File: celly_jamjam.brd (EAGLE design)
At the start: 100 x 80 mm, 58 parts, among them T1 2N3904, U1 OSCILLATOR5X3

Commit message: finished schematic, now onto board. jeeez
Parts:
- removed ICL7660: (no value), ic-package:DIL08
- added FERRITEBEADLEAD: type43, inductors:0402
- added IC1: M3500-1324S/T, burr-brown:SOT23-5
- added MICROSTRIPLINE, MICROSTRIPLN2: 50 Ohm, inductors:0402
- added RFOUTPUTANTENNA: 80mW, SparkFun-RF:ANTENNA-CHIP
- moved 1MEG 285.1 mm to (96.5, 58.4)
- moved C22 275.8 mm to (88.9, 71.1)
- moved C23 275.8 mm to (88.9, 40.6)
- moved NOISEAMP 275.8 mm to (88.9, 30.5)
- moved R23 275.8 mm to (87.6, 74.9)
- moved R24 275.8 mm to (87.6, 67.3)
- moved R25 275.8 mm to (87.6, 63.5)
- moved R28 275.8 mm to (88.9, 45.7)
- moved L2 255.5 mm to (52.1, 6.35)
- moved U1 247.7 mm to (67.3, 3.81), turned to 180 degrees
- moved TRANSISTOR 243.0 mm to (31.8, 6.35)
- moved SWEEPAMP 239.0 mm to (94.0, 11.4), turned to 180 degrees
- moved LM1458 237.0 mm to (55.9, 71.1)
- moved TRIWAVGEN 196.7 mm to (95.2, 3.81), turned to 90 degrees
- moved C1 186.5 mm to (69.8, 80.0)
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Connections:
- new net N$33: C9.1, IC1.3
- new net N$34: MICROSTRIPLN2.2, RFOUTPUTANTENNA.FEED
- new net N$35: C9.2, MICROSTRIPLINE.2
- new net N$36: FERRITEBEADLEAD.2, R16.1
- new net N$37: MICROSTRIPLN2.1
- net GND: now also IC1.2, IC1.5, RFOUTPUTANTENNA.GND; no longer ICL7660.3
- net N$17: now also IC1.1
- net N$2: now also FERRITEBEADLEAD.1; no longer R16.1
- net N$28: now also MICROSTRIPLINE.1
- net N$4: now also C17.A, VOLTAGEINVERT.2; no longer C17.C, ICL7660.4
- net N$5: now also C17.C, VOLTAGEINVERT.4; no longer C17.A, ICL7660.2
- net N$7: now also VOLTAGEINVERT.5; no longer ICL7660.5
- net V+: no longer VOLTAGEINVERT.8
- net VCC: now also VOLTAGEINVERT.1, VOLTAGEINVERT.8; no longer ICL7660.1, ICL7660.8
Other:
- board size 100 x 80 mm -> 100 x 82.5 mm

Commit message: design is better
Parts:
- removed MICROSTRIPLN2: 50 Ohm, inductors:0402
- removed TRANSISTOR: MPF102, transistor-small-signal:SOT23
- added MICROSTRIPLINE1: 50 Ohm, inductors:0402
- added Q1: mpf102, transistor-fet:TO92
- C10, C9: value (none) -> 68pF
- C12: value (none) -> 0.1uF
- IC1: value M3500-1324S/T -> AG603-86
- U1: value OSCILLATOR5X3 -> M3500
- moved TRIWAVGEN 84.6 mm to (39.5, 67.5)
- moved 1MEG 82.2 mm to (14.8, 68.1), turned to 90 degrees
- moved RFOUTPUTANTENNA 74.1 mm to (78.6, 38.5), turned to 180 degrees
- moved R25 68.4 mm to (19.4, 68.2), turned to 90 degrees
- moved SWEEPAMP 68.1 mm to (45.9, 59.7)
- moved C19 66.5 mm to (20.6, 72.5), turned to 270 degrees
- moved R3 61.3 mm to (28.3, 69.1), turned to 180 degrees
- moved C18 60.3 mm to (25.5, 72.5), turned to 270 degrees
- moved C2 59.4 mm to (17.1, 50.2), turned to 180 degrees
- moved L1 58.9 mm to (71.3, 42.4), turned to 90 degrees
- moved C1 58.0 mm to (14.8, 61.5), turned to 270 degrees
- moved NOISEAMP 57.7 mm to (35.0, 51.1), turned to 90 degrees
- moved C16 56.7 mm to (16.0, 53.9), turned to 180 degrees
- moved IC1 56.6 mm to (66.1, 55.1), turned to 270 degrees
- moved L2 56.3 mm to (61.2, 61.9), turned to 90 degrees
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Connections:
- removed net N$34 (its old number): MICROSTRIPLN2.2, RFOUTPUTANTENNA.FEED
- removed net N$37: MICROSTRIPLN2.1
- new net N$17: C10.1, MICROSTRIPLINE1.1
- new net N$40: MICROSTRIPLINE1.2, RFOUTPUTANTENNA.FEED
- net N$24: now also Q1.3; no longer TRANSISTOR.3
- net N$27: now also Q1.1; no longer TRANSISTOR.1
- net N$30: now also Q1.2; no longer TRANSISTOR.2
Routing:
- net GND: track 0.00 -> 44.6 mm
- net VCC: track 0.00 -> 26.6 mm
- net N$3: track 0.00 -> 21.0 mm
- net N$13: track 0.00 -> 20.5 mm
- net N$32: track 0.00 -> 15.6 mm
- net N$36: track 0.00 -> 12.8 mm
- net N$24: track 0.00 -> 11.4 mm
- net N$19: track 0.00 -> 11.3 mm
- net N$26: track 0.00 -> 9.98 mm
- net N$14: track 0.00 -> 9.51 mm
- net N$34: track 0.00 -> 9.41 mm
- net N$2: track 0.00 -> 9.09 mm
- net N$20: track 0.00 -> 8.79 mm
- net N$8: track 0.00 -> 8.28 mm
- net N$27: track 0.00 -> 8.14 mm
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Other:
- board size 100 x 82.5 mm -> 117.8 x 83.8 mm

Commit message: added correct VCO
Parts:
- removed C5: 0.1uF, SparkFun-Passives:0603-CAP
- removed U1: M3500, SparkFun-FreqCtrl:CRYSTAL-SMD-5X3
- added C24: 0.1uF, SparkFun-Passives:0603-CAP
- added U$1: CVCO55CL, crystec_vco:CVCO55CL
- L1: value 10uH -> 10nh
- moved L1 62.0 mm to (15.5, 15.5), turned to 0 degrees
- moved C6 55.8 mm to (21.5, 15.5), turned to 0 degrees
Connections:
- new net N$37: C24.2, L1.2, U$1.P$14
- net GND: now also C24.1, C6.1, U$1.P$7; no longer C5.1, C6.2, U1.2
- net N$29: no longer U1.3
- net N$3: now also U$1.P$10; no longer C20.A, C6.1, L1.2, U1.4
- net N$32: now also U$1.P$2; no longer U1.1
- net VCC: now also C20.A, C6.2; no longer C5.2
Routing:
- net N$3: track 21.0 -> 0.00 mm
- net VCC: track 26.6 -> 19.3 mm
- net N$16: track 0.00 -> 5.30 mm
- net GND: track 44.6 -> 40.6 mm

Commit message: added VCO, changed design. still needs a lot of work
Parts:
- moved C6 31.3 mm to (14.5, 46.0), turned to 180 degrees
- moved L1 22.1 mm to (14.0, 37.5), turned to 90 degrees
- moved C24 20.6 mm to (20.5, 41.0), turned to 180 degrees
- moved U$1 7.00 mm to (18.5, 21.5)
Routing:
- net N$32: track 15.5 -> 55.2 mm
- net VCC: track 19.3 -> 39.5 mm
- net N$37: track 0.00 -> 18.7 mm
- net GND: track 40.6 -> 41.4 mm
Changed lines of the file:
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@@
 <element name="C10" library="SparkFun-Passives" package="0603-CAP" value="68pF" x="64.5" y="59" rot="R180"/>
 <element name="Q1" library="transistor-fet" package="TO92" value="mpf102" x="51" y="47"/>
-<element name="U$1" library="crystec_vco" package="CVCO55CL" value="CVCO55CL" x="18.5" y="28.5"/>
-<element name="C24" library="SparkFun-Passives" package="0603-CAP" value="0.1uF" x="10.5" y="23"/>
-<element name="C6" library="SparkFun-Passives" package="0603-CAP" value="0.1uF" x="21.5" y="15.5"/>
-<element name="L1" library="SparkFun-Passives" package="0603" value="10nh" x="15.5" y="15.5"/>
+<element name="U$1" library="crystec_vco" package="CVCO55CL" value="CVCO55CL" x="18.5" y="21.5"/>
+<element name="C24" library="SparkFun-Passives" package="0603-CAP" value="0.1uF" x="20.5" y="41" rot="R180"/>
+<element name="C6" library="SparkFun-Passives" package="0603-CAP" value="0.1uF" x="14.5" y="46" rot="R180"/>
+<element name="L1" library="SparkFun-Passives" package="0603" value="10nh" x="14" y="37.5" rot="R90"/>
 </elements>
 <signals>
@@
 <wire x1="26.8534" y1="52.575" x2="34.21" y2="55.21" width="0" layer="19" extent="1-1"/>
 <wire x1="19.41" y1="58.82" x2="26.8534" y2="52.575" width="0" layer="19" extent="1-1"/>
+<wire x1="15.35" y1="46" x2="15.28" y2="50.22" width="0" layer="19" extent="1-1"/>
 <wire x1="44.345" y1="35.09" x2="40.52" y2="46.45" width="0" layer="19" extent="1-1"/>
 <wire x1="45.615" y1="35.09" x2="44.345" y2="35.09" width="0" layer="19" extent="1-1"/>
+<wire x1="31.2" y1="29.247" x2="44.345" y2="35.09" width="0" layer="19" extent="1-1"/>
 <wire x1="20.62" y1="73.88" x2="14.85" y2="60.64" width="0" layer="19" extent="1-1"/>
-<wire x1="31.2" y1="36.247" x2="44.345" y2="35.09" width="0" layer="19" extent="1-1"/>
-<wire x1="9.65" y1="23" x2="31.2" y2="36.247" width="0" layer="19" extent="1-1"/>
-<wire x1="20.65" y1="15.5" x2="9.65" y2="23" width="0" layer="19" extent="1-1"/>
+<wire x1="21.35" y1="41" x2="21.5" y2="41" width="0.4064" layer="1"/>
+<wire x1="21.5" y1="41" x2="22" y2="41.5" width="0.4064" layer="1"/>
+<wire x1="22" y1="41.5" x2="15.35" y2="46" width="0" layer="19" extent="1-16"/>
 </signal>
 <signal name="VCC">
@@
 <contactref element="C6" pad="2"/>
 <contactref element="C20" pad="A"/>
+<wire x1="18.135" y1="50.035" x2="18.135" y2="48.135" width="0.4064" layer="1"/>
+<wire x1="18.135" y1="48.135" x2="18" y2="48" width="0.4064" layer="1"/>
+<wire x1="18" y1="48" x2="13.5" y2="48" width="0.4064" layer="1"/>
+<wire x1="13.5" y1="48" x2="13.5" y2="46.15" width="0.4064" layer="1"/>
+<wire x1="13.5" y1="46.15" x2="13.65" y2="46" width="0.4064" layer="1"/>
+<wire x1="13.65" y1="46" x2="13.65" y2="41.15" width="0.4064" layer="1"/>
+<wire x1="13.65" y1="41.15" x2="12.5" y2="40" width="0.4064" layer="1"/>
+<wire x1="12.5" y1="40" x2="12.5" y2="36.5" width="0.4064" layer="1"/>
+<wire x1="12.5" y1="36.5" x2="13.85" y2="36.5" width="0.4064" layer="1"/>
+<wire x1="13.85" y1="36.5" x2="14" y2="36.65" width="0.4064" layer="1"/>
 <wire x1="71.17" y1="49.015" x2="67.52" y2="60.76" width="0" layer="19" extent="1-1"/>
 <wire x1="72.78" y1="46.89" x2="71.17" y2="49.015" width="0" layer="19" extent="1-1"/>
@@
 <wire x1="30.82" y1="64.84" x2="26.8534" y2="50.035" width="0" layer="19" extent="1-1"/>
 <wire x1="30.94" y1="71.06" x2="30.94" y2="64.96" width="0" layer="19" extent="1-1"/>
-<wire x1="22.35" y1="15.5" x2="47.99" y2="30.2" width="0" layer="19" extent="1-1"/>
-<wire x1="14.65" y1="15.5" x2="22.35" y2="15.5" width="0" layer="19" extent="1-1"/>
 </signal>
 <signal name="V+">
@@
 <contactref element="C3" pad="2"/>
 <contactref element="R3" pad="1"/>
-<wire x1="29.16" y1="69.09" x2="30.82" y2="59.76" width="0" layer="19" extent="1-1"/>
 <wire x1="36.1" y1="60.14" x2="31.2" y2="60.14" width="0.4064" layer="1"/>
 <wire x1="31.2" y1="60.14" x2="30.82" y2="59.76" width="0.4064" layer="1"/>
 <wire x1="40.17" y1="60.14" x2="36.1" y2="60.14" width="0.4064" layer="1"/>
+<wire x1="31.2" y1="60.14" x2="29.16" y2="69.09" width="0" layer="19" extent="1-1"/>
 </signal>
 <signal name="N$8">
@@
 <contactref element="1MEG" pad="8"/>
 <contactref element="1MEG" pad="6"/>
-<wire x1="19.39" y1="69.04" x2="23.2" y2="64.84" width="0" layer="19" extent="1-1"/>
+<wire x1="27.46" y1="69.09" x2="23.59" y2="69.09" width="0.4064" layer="1"/>
+<wire x1="23.59" y1="69.09" x2="23.5" y2="69" width="0.4064" layer="1"/>
+<wire x1="23.5" y1="69" x2="23.5" y2="65.14" width="0.4064" layer="1"/>
+<wire x1="23.5" y1="65.14" x2="23.2" y2="64.84" width="0.4064" layer="1"/>
 <wire x1="15.475" y1="69.27" x2="19.39" y2="69.04" width="0" layer="19" extent="1-1"/>
 <wire x1="15.475" y1="68.47" x2="15.475" y2="69.27" width="0" layer="19" extent="1-1"/>
@@
 <wire x1="14.225" y1="67.67" x2="14.225" y2="68.47" width="0" layer="19" extent="1-1"/>
 <wire x1="14.225" y1="66.87" x2="14.225" y2="67.67" width="0" layer="19" extent="1-1"/>
-<wire x1="27.46" y1="69.09" x2="23.59" y2="69.09" width="0.4064" layer="1"/>
-<wire x1="23.59" y1="69.09" x2="23.5" y2="69" width="0.4064" layer="1"/>
-<wire x1="23.5" y1="69" x2="23.5" y2="65.14" width="0.4064" layer="1"/>
-<wire x1="23.5" y1="65.14" x2="23.2" y2="64.84" width="0.4064" layer="1"/>
+<wire x1="23.5" y1="69" x2="19.39" y2="69.04" width="0" layer="19" extent="1-1"/>
 </signal>
 <signal name="N$10">
@@
 <contactref element="R18" pad="1"/>
 <contactref element="T1" pad="2"/>
-<wire x1="56.93" y1="29.23" x2="58.05" y2="33.595" width="0" layer="19" extent="1-1"/>
 <wire x1="53.82" y1="32.27" x2="53.82" y2="30.68" width="0.4064" layer="1"/>
 <wire x1="53.82" y1="30.68" x2="54" y2="30.5" width="0.4064" layer="1"/>
 <wire x1="54" y1="30.5" x2="55.66" y2="30.5" width="0.4064" layer="1"/>
 <wire x1="55.66" y1="30.5" x2="56.93" y2="29.23" width="0.4064" layer="1"/>
+<wire x1="55.66" y1="30.5" x2="58.05" y2="33.595" width="0" layer="19" extent="1-1"/>
 </signal>
 <signal name="N$21">
@@
 <contactref element="C15" pad="1"/>
 <contactref element="NOISEAMP" pad="2"/>
-<wire x1="35.605" y1="50.73" x2="38.13" y2="50.71" width="0" layer="19" extent="1-1"/>
 <wire x1="40.89" y1="49.79" x2="40.89" y2="50.11" width="0.4064" layer="1"/>
 <wire x1="40.89" y1="50.11" x2="40" y2="51" width="0.4064" layer="1"/>
 <wire x1="40" y1="51" x2="38.42" y2="51" width="0.4064" layer="1"/>
 <wire x1="38.42" y1="51" x2="38.13" y2="50.71" width="0.4064" layer="1"/>
+<wire x1="35.605" y1="50.73" x2="38.13" y2="50.71" width="0" layer="19" extent="1-1"/>
 </signal>
 <signal name="N$24">
@@
 <wire x1="56.96" y1="46.5" x2="56.92" y2="46.54" width="0.4064" layer="1"/>
 <contactref element="U$1" pad="P$2"/>
-<wire x1="23.961" y1="28.5" x2="52" y2="43.04" width="0" layer="19" extent="1-1"/>
+<wire x1="23.961" y1="21.5" x2="35" y2="21.5" width="0.4064" layer="1"/>
+<wire x1="35" y1="21.5" x2="51.5" y2="38" width="0.4064" layer="1"/>
+<wire x1="51.5" y1="38" x2="51.5" y2="42.54" width="0.4064" layer="1"/>
+<wire x1="51.5" y1="42.54" x2="52" y2="43.04" width="0.4064" layer="1"/>
 </signal>
 <signal name="N$31">
@@
 <contactref element="VOLTAGEINVERT" pad="5"/>
 <contactref element="LM1458" pad="4"/>
-<wire x1="20.7066" y1="53.845" x2="23.2" y2="57.22" width="0" layer="19" extent="1-1"/>
 <wire x1="20.7066" y1="53.845" x2="17.445" y2="53.845" width="0.4064" layer="1"/>
 <wire x1="17.445" y1="53.845" x2="17.39" y2="53.9" width="0.4064" layer="1"/>
+<wire x1="20.7066" y1="53.845" x2="23.2" y2="57.22" width="0" layer="19" extent="1-1"/>
 </signal>
 <signal name="N$17">
@@
 <contactref element="C4" pad="1"/>
 <contactref element="Q1" pad="2"/>
-<wire x1="51" y1="48.905" x2="56.92" y2="48.24" width="0" layer="19" extent="1-1"/>
 <wire x1="46.83" y1="53.13" x2="48.37" y2="53.13" width="0.4064" layer="1"/>
 <wire x1="48.37" y1="53.13" x2="51" y2="50.5" width="0.4064" layer="1"/>
 <wire x1="51" y1="50.5" x2="51" y2="48.905" width="0.4064" layer="1"/>
+<wire x1="51" y1="48.905" x2="56.92" y2="48.24" width="0" layer="19" extent="1-1"/>
 </signal>
 <signal name="N$27">
@@
 <contactref element="L1" pad="2"/>
 <contactref element="U$1" pad="P$14"/>
-<wire x1="11.35" y1="23" x2="16.35" y2="15.5" width="0" layer="19" extent="1-1"/>
-<wire x1="18.5" y1="36.501" x2="11.35" y2="23" width="0" layer="19" extent="1-1"/>
+<wire x1="19.65" y1="41" x2="16.65" y2="41" width="0.4064" layer="1"/>
+<wire x1="16.65" y1="41" x2="14" y2="38.35" width="0.4064" layer="1"/>
+<wire x1="14" y1="38.35" x2="14.65" y2="38.35" width="0.4064" layer="1"/>
+<wire x1="14.65" y1="38.35" x2="17" y2="36" width="0.4064" layer="1"/>
+<wire x1="17" y1="36" x2="17" y2="29.5" width="0.4064" layer="1"/>
+<wire x1="17" y1="29.5" x2="18.499" y2="29.5" width="0.4064" layer="1"/>
+<wire x1="18.499" y1="29.5" x2="18.5" y2="29.501" width="0.4064" layer="1"/>
 </signal>
 <signal name="N$3">

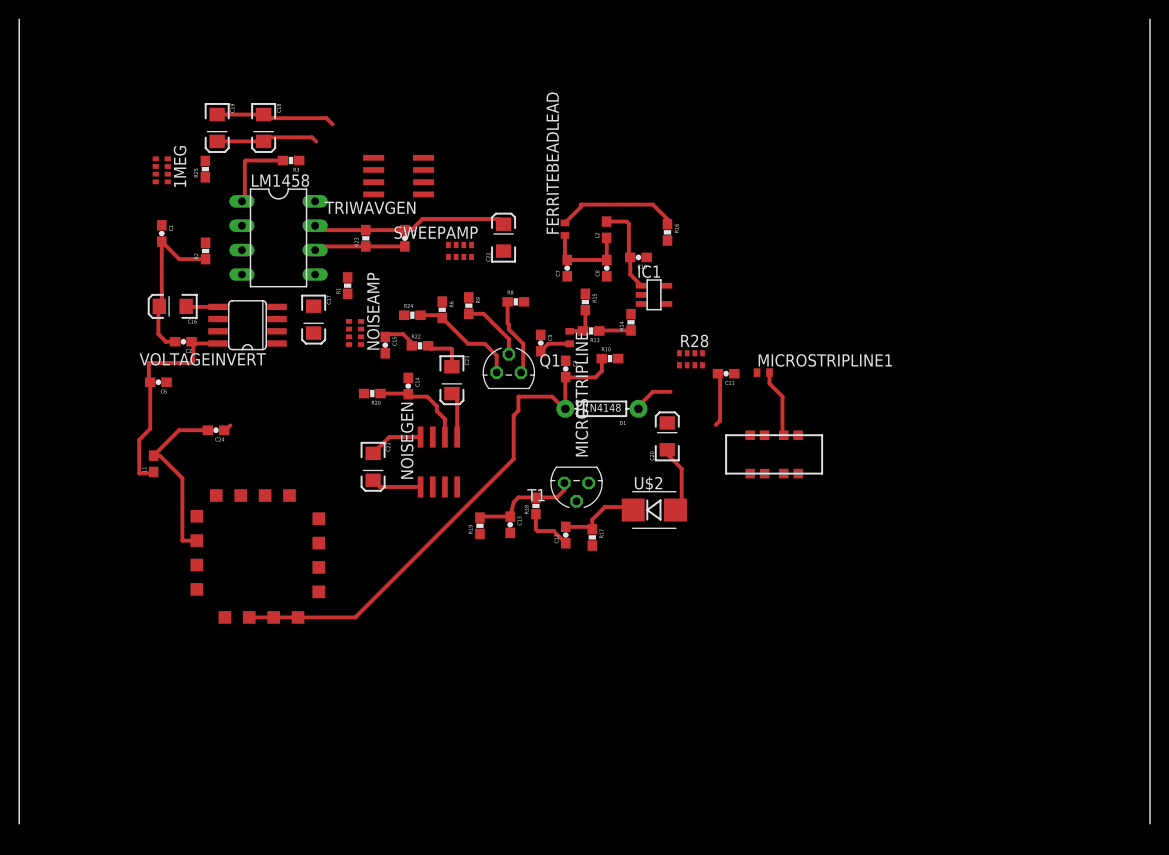
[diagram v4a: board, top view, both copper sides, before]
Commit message: changed everything to SMD. much work to be done
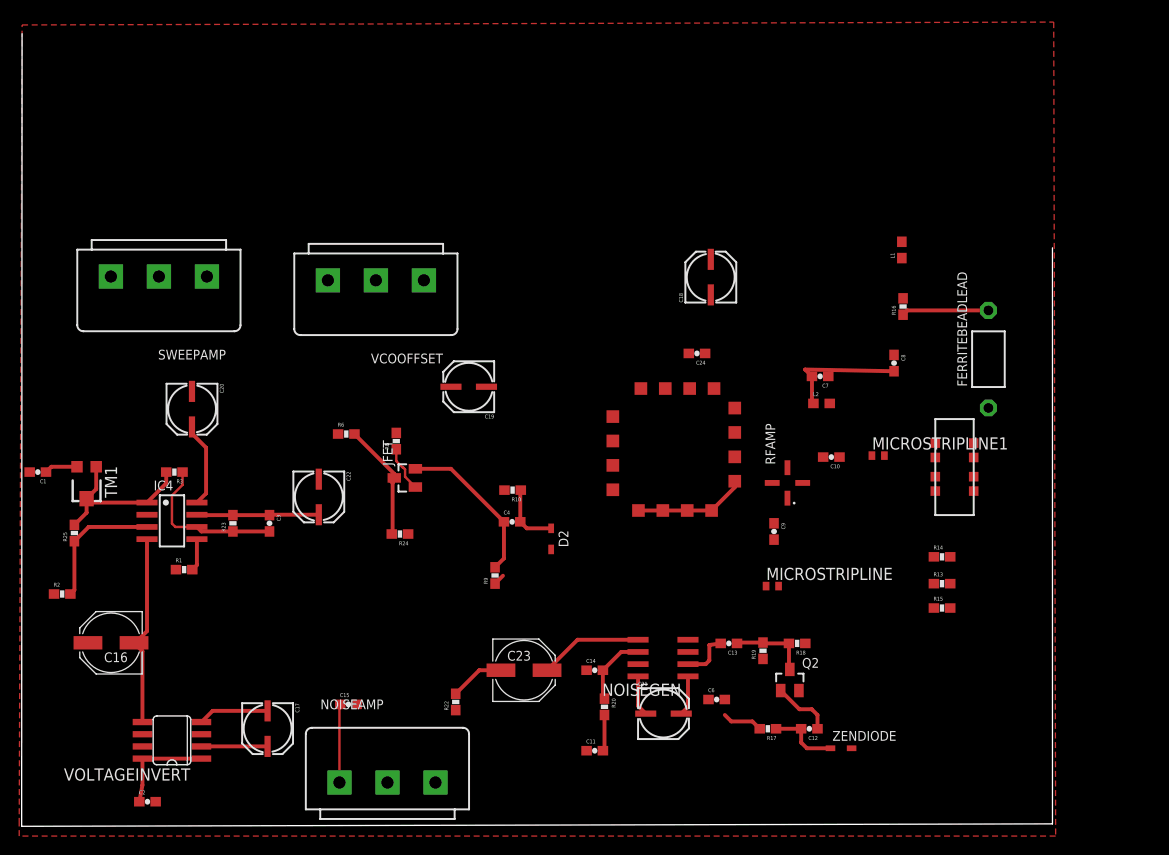
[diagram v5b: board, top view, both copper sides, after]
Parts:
- removed 1MEG, R28: POTENTIOMETER, SparkFun-Passives:0603-ARV
- removed D1: 1N4148, SparkFun-DiscreteSemi:DIODE-1N4148
- removed IC1: AG603-86, burr-brown:SOT23-5
- removed LM1458: (no value), ic-package:DIL08
- removed Q1: mpf102, transistor-fet:TO92
- removed T1: 2N3904, transistor:TO92
- removed TRIWAVGEN: LM1458D, linear:SO08
- removed U$2: DIODE-ZENERSMB, SparkFun-DiscreteSemi:SMB-DIODE
- added D2: 1N4148, zetex:SOD323
- added IC4: LM1458, linear:SO08
- added JFET: MMBF5484*, transistor-fet:SOT23
- added Q2: MMBT3904, transistor-npn:SOT23-BEC
- added RFAMP: ag603, mini-circuits:FG873
- added TM1: (no value), adafruit:TC33X
- added VCOOFFSET: 5K/10TURN, pot:P160KN
- added ZENDIODE: MMBZ5235BW, zetex:SOD323
- C16, C23: device SparkFun-Capacitors:EIA3216 -> SparkFun-Capacitors:PANASONIC_D
- C17, C18, C19, C20, C21, C22: device SparkFun-Capacitors:EIA3216 -> SparkFun-Capacitors:PANASONIC_C
- FERRITEBEADLEAD: device inductors:0402 -> inductor-jwmiller:FB-226
- NOISEAMP: value 5k/10turn -> 5K/10TURN; device SparkFun-Passives:0603-ARV -> pot:P160KN
- NOISEGEN: device linear:SO08 -> linear:SO08@1
- SWEEPAMP: device SparkFun-Passives:0603-ARV -> pot:P160KN
- moved L1 81.1 mm to (91.9, 59.8)
- moved C6 66.9 mm to (72.6, 13.0), turned to 0 degrees
- moved NOISEAMP 50.7 mm to (38.4, 0.51), turned to 270 degrees
- moved C24 50.7 mm to (70.6, 49.0)
- moved U$1 49.5 mm to (61.8, 45.3), turned to 270 degrees
- moved C20 49.4 mm to (18.2, 43.2), turned to 270 degrees
- moved R15 49.0 mm to (96.1, 22.5), turned to 0 degrees
- moved C18 48.9 mm to (71.8, 56.9), turned to 90 degrees
- moved C2 48.1 mm to (13.4, 2.31), turned to 0 degrees
- moved FERRITEBEADLEAD 46.1 mm to (100.9, 48.4)
- moved R13 45.0 mm to (96.1, 25.0), turned to 0 degrees
- moved VOLTAGEINVERT 44.0 mm to (15.9, 8.70)
- moved C17 42.8 mm to (26.1, 9.97)
- moved C11 41.6 mm to (59.9, 7.62), turned to 0 degrees
- moved R20 40.6 mm to (61.0, 12.2), turned to 270 degrees
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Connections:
- removed net N$1: LM1458.5, R1.2
- removed net N$13: C22.A, C3.1, LM1458.7, R23.2
- removed net N$9: LM1458.3, R2.2, R25.1
- removed net V+: TRIWAVGEN.8
- removed net V-: TRIWAVGEN.4
- new net N$47: JFET.3, R24.2, R6.2
- new net N$48: IC4.5, R1.2
- new net N$49: IC4.3, R2.2, R25.1
- new net VDD: C20.+, C6.2, L1.1
- net GND: now also C16.+, C18.-, C19.-, C20.-, D2.2, NOISEAMP.3, Q2.E, RFAMP.2, RFAMP.4, SWEEPAMP.1, U$1.P$1, U$1.P$11, U$1.P$12, U$1.P$13, U$1.P$15, U$1.P$16, U$1.P$3, U$1.P$4, U$1.P$5, U$1.P$6, U$1.P$8, U$1.P$9, VCOOFFSET.3, ZENDIODE.2; no longer C16.A, C18.C, C19.C, C20.C, D1.A, IC1.2, IC1.5, NOISEAMP.1, R28.2, SWEEPAMP.2, T1.3, U$2.A
- net N$10: now also IC4.2, TM1.3; no longer 1MEG.1, LM1458.2
- net N$11: now also SWEEPAMP.2; no longer SWEEPAMP.3, SWEEPAMP.4, SWEEPAMP.5, SWEEPAMP.6, SWEEPAMP.7, SWEEPAMP.8
- net N$12: now also C22.-, SWEEPAMP.3; no longer C22.C, SWEEPAMP.1
- net N$14: now also IC4.6; no longer LM1458.6
- net N$15: now also C21.-; no longer C21.C
- net N$16: now also Q2.B; no longer T1.2
- net N$19: now also Q2.C; no longer T1.1
- net N$20: now also ZENDIODE.1; no longer U$2.C
- net N$21: now also C23.-; no longer C23.C
- net N$22: now also C23.+; no longer C23.A
- net N$23: now also NOISEAMP.1; no longer NOISEAMP.2
- net N$24: now also C22.+, C3.1, IC4.7, R23.2; no longer Q1.3, R24.2, R6.2
- net N$25: now also NOISEAMP.2; no longer NOISEAMP.3, NOISEAMP.4, NOISEAMP.5, NOISEAMP.6, NOISEAMP.7, NOISEAMP.8
- net N$27: now also JFET.1; no longer Q1.1
- net N$30: now also JFET.2; no longer Q1.2
- net N$31: now also VCOOFFSET.2; no longer R28.3, R28.4, R28.5, R28.6, R28.7, R28.8
- net N$32: now also D2.1; no longer D1.C
- net N$33: now also RFAMP.1; no longer IC1.3
- net N$34: now also RFAMP.3; no longer IC1.1
- net N$4: now also C17.+; no longer C17.A
- net N$5: now also C17.-; no longer C17.C
- net N$6: now also C21.+; no longer C21.A
- net N$7: now also C16.-, IC4.4; no longer C16.C, LM1458.4
- net N$8: now also IC4.1, TM1.1, TM1.2; no longer 1MEG.2, 1MEG.3, 1MEG.4, 1MEG.5, 1MEG.6, 1MEG.7, 1MEG.8, LM1458.1
- net VCC: now also C18.+, C19.+, IC4.8, VCOOFFSET.1; no longer C18.A, C19.A, C20.A, C6.2, L1.1, LM1458.8, R28.1
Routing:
- net N$32: track 55.2 -> 6.82 mm
- net GND: track 41.4 -> 13.6 mm
- net N$13: track 20.5 -> 0.00 mm
- net N$37: track 18.7 -> 0.00 mm
- net N$7: track 3.34 -> 19.9 mm
- net N$49: track 0.00 -> 13.8 mm
- net N$47: track 0.00 -> 12.5 mm
- net VCC: track 39.5 -> 27.1 mm
- net N$30: track 6.85 -> 16.6 mm
- net N$34: track 9.41 -> 0.00 mm
- net N$8: track 8.28 -> 17.5 mm
- net N$5: track 0.00 -> 7.37 mm
- net N$40: track 7.13 -> 0.00 mm
- net N$4: track 0.00 -> 6.89 mm
- net N$14: track 9.51 -> 16.3 mm
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- added copper zone on layer 1, net GND
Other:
- board size 117.8 x 83.8 mm -> 107.4 x 82.6 mm
